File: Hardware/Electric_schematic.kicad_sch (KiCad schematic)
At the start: 10 parts, among them P1 Mains_Connector, SW1 ON/OFF, U1 SSR

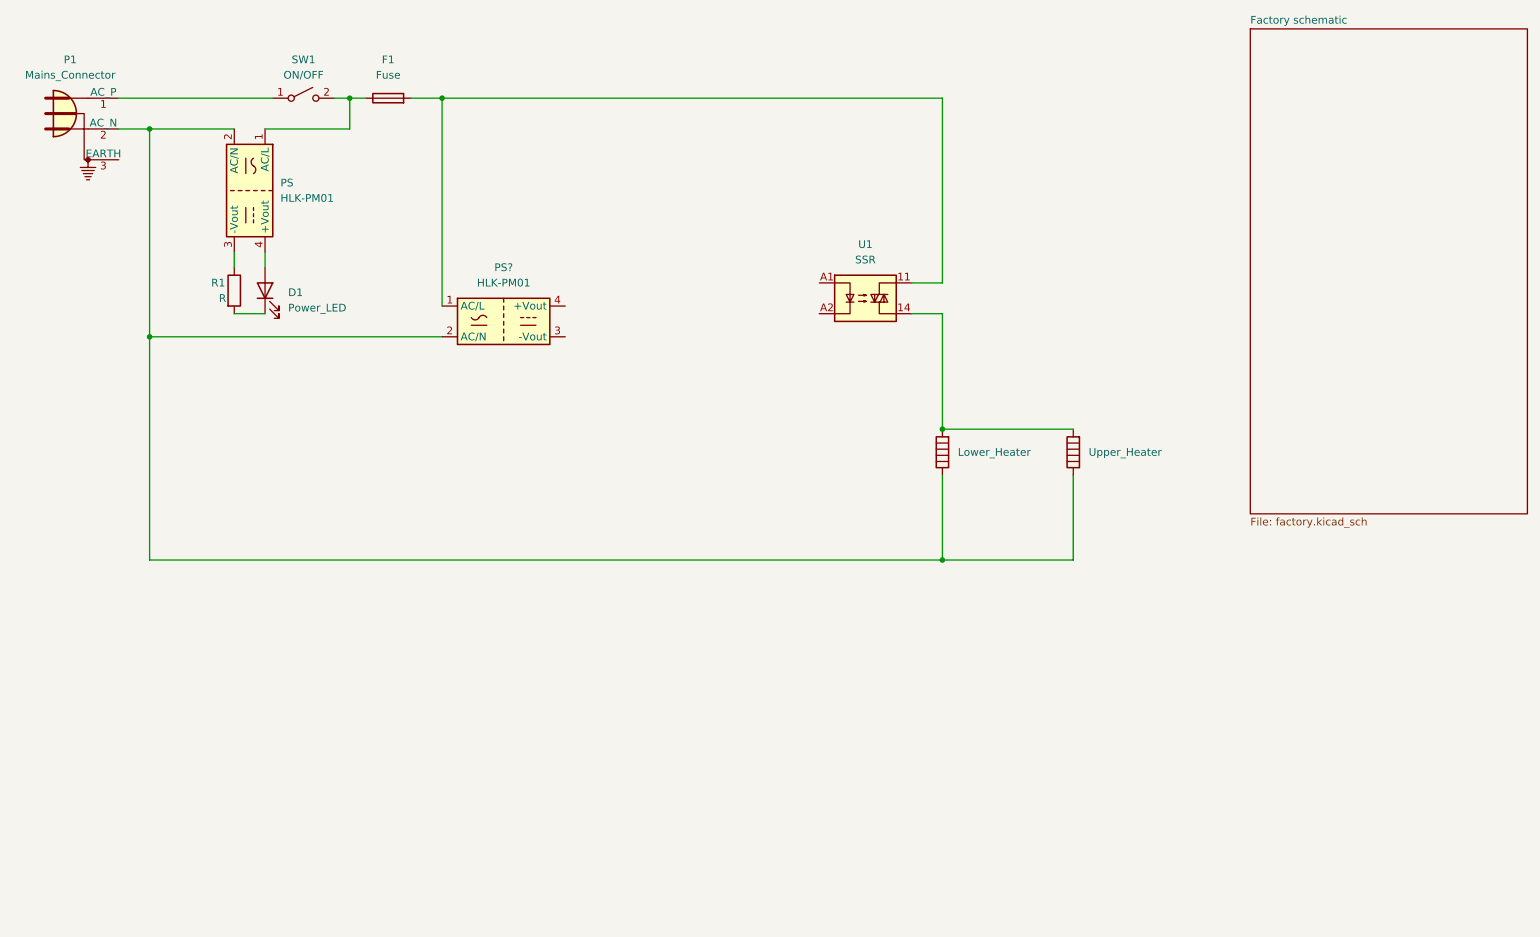
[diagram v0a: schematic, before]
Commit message: Electrical schematic functionally complete, not added fuse rating
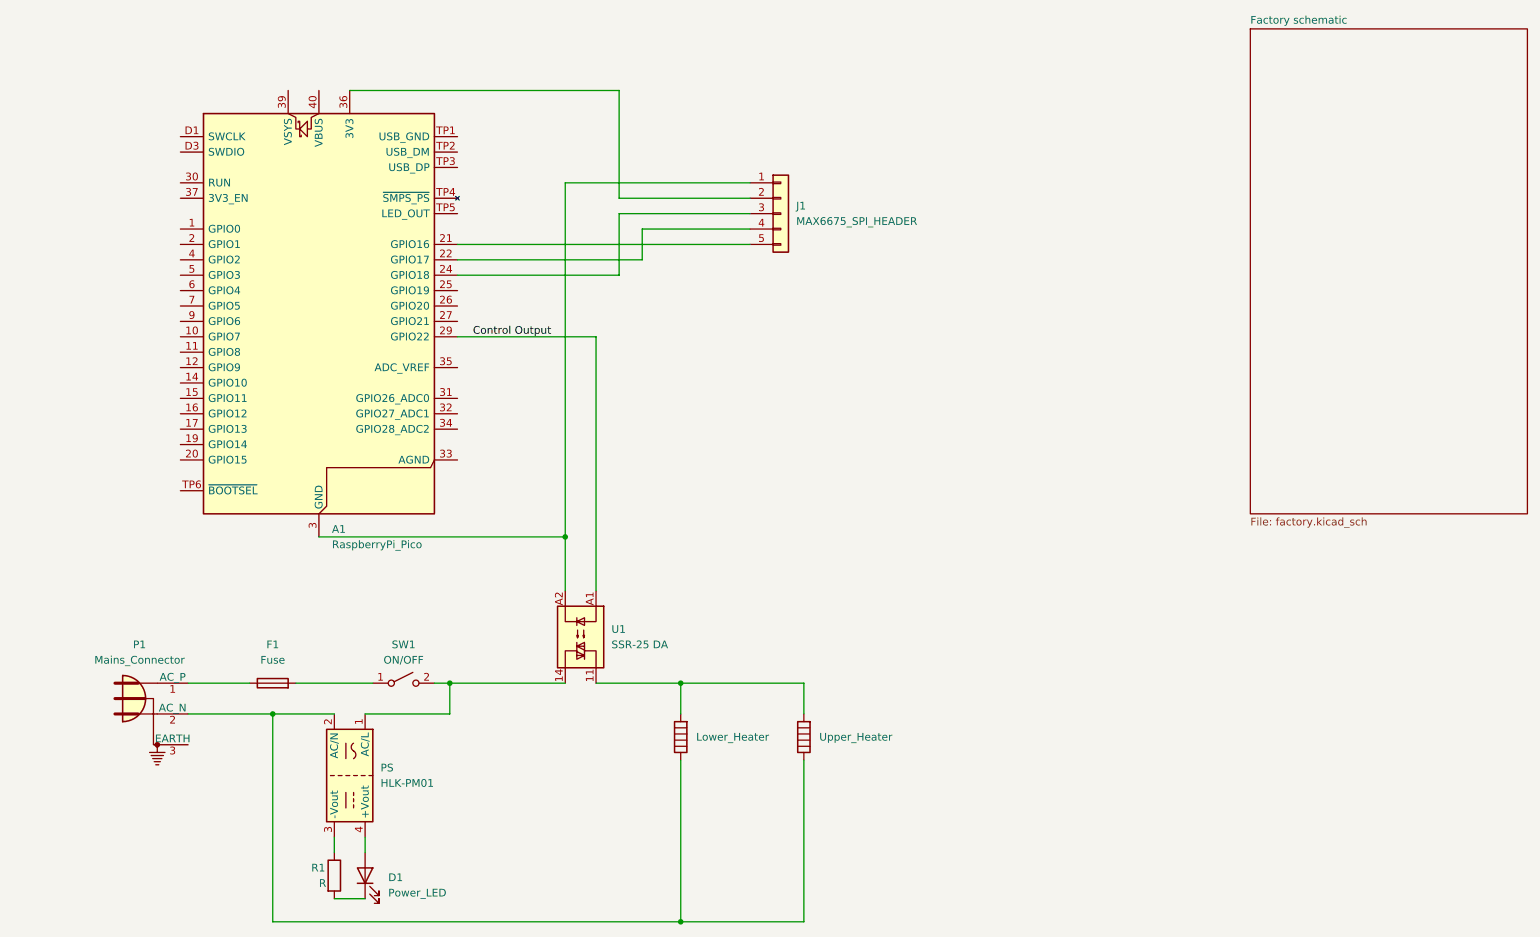
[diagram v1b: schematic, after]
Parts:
- removed PS?: HLK-PM01, Converter_ACDC:Converter_ACDC_HiLink_HLK-PMxx, symbol Converter_ACDC:HLK-PM01
- added A1: RaspberryPi_Pico, Module:RaspberryPi_Pico_SMD, symbol MCU_Module:RaspberryPi_Pico_Extensive
- added J1: MAX6675_SPI_HEADER, symbol Connector_Generic:Conn_01x05
- U1: value SSR -> SSR-25 DA
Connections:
- net at Lower_Heater.2, Upper_Heater.2: now also U1.11; no longer U1.14
- net at SW1.1 (A): now also F1.2; no longer P1.1 (AC_P)
- net at PS.1 (AC/L), SW1.2 (B): now also U1.14; no longer F1.1
- net Control Output: now reaches U1.A1
- net Control Output: now also A1.29 (GPIO22)
- net at U1.A2: now also A1.13 (GND), A1.18 (GND), A1.23 (GND), A1.28 (GND), A1.3 (GND), A1.38 (GND), A1.8 (GND), A1.D2 (GND), J1.1 (Pin_1)
- new net: F1.1, P1.1 (AC_P)
- new net: A1.21 (GPIO16), J1.5 (Pin_5)
- new net: A1.22 (GPIO17), J1.4 (Pin_4)
- new net: A1.24 (GPIO18), J1.3 (Pin_3)
- new net: A1.36 (3V3), J1.2 (Pin_2)
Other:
- moved on the sheet: D1, F1, Lower_Heater, P1, PS, R1, SW1, U1, Upper_Heater
